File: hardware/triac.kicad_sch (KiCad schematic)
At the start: 23 parts, among them Q2 BTA16-600B, Q3 BC848, U4 TL082

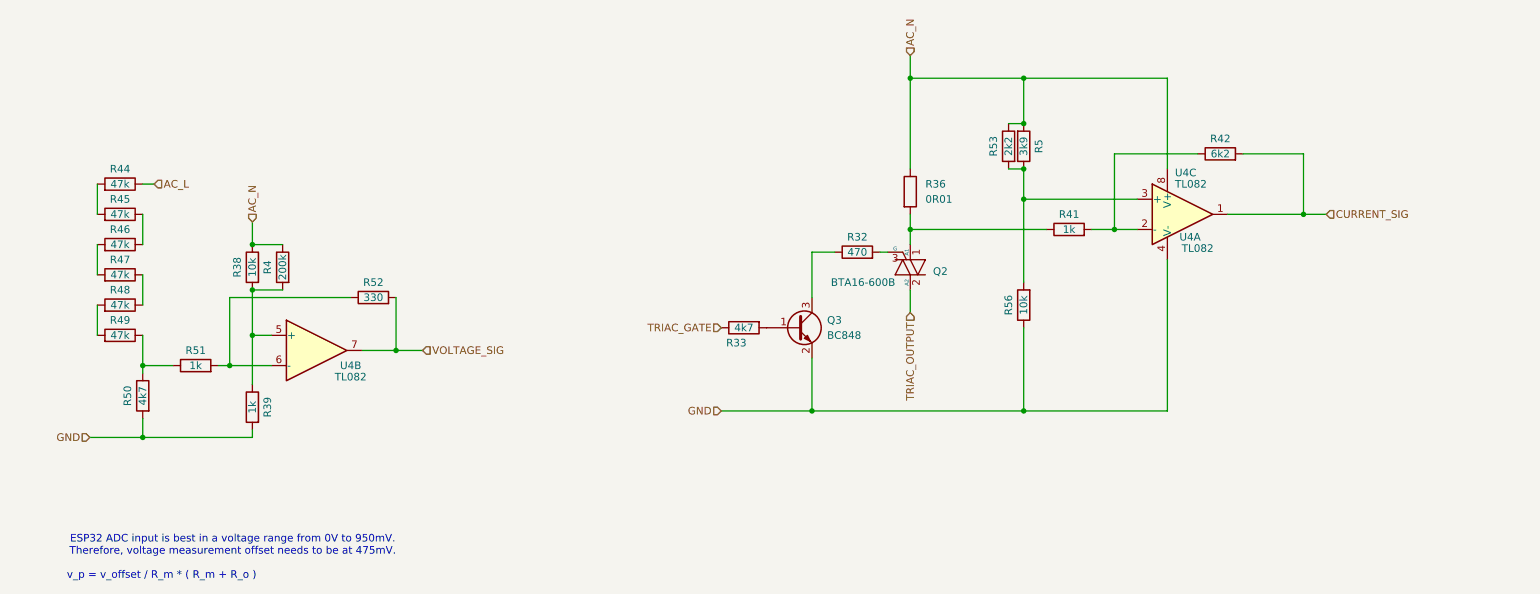
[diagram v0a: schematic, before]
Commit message: bugfix: triac output needs to confront L potential
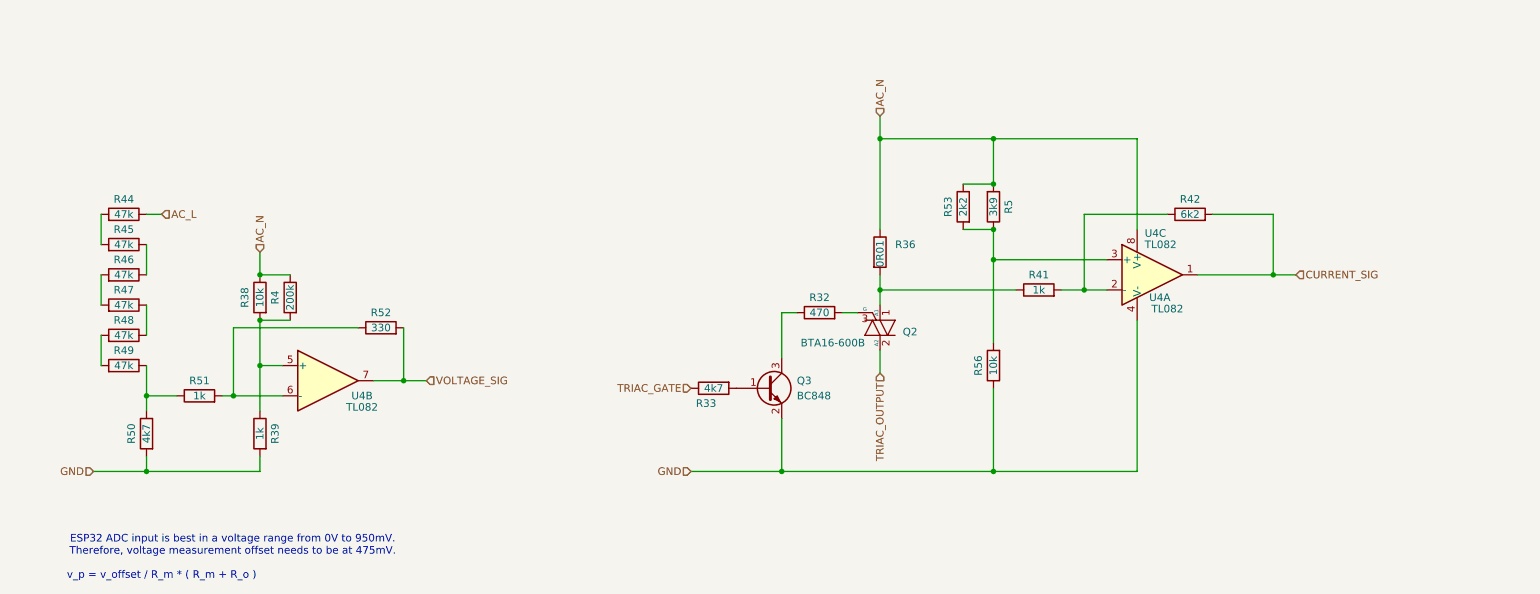
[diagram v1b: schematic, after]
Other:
- moved on the sheet: Q2, Q3, R32, R33, R36, R38, R39, R4, R41, R42, R44, R45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

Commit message: added some datasheets
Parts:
- removed R44, R45, R46, R47, R48, R49: 47k, Resistor_SMD:R_0603_1608Metric, symbol Device:R
- added R6: 270k, Resistor_SMD:R_MELF_MMB-0207, symbol Device:R
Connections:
- net AC_L: now also R6.1
- net at R50.1, R51.1: now also R6.2
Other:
- moved on the sheet: R36

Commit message: some more rules and routings
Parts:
- removed Q3: BC848, Package_TO_SOT_SMD:SOT-23, symbol Transistor_BJT:BC848
- removed R33: 4k7, Resistor_SMD:R_0603_1608Metric, symbol Device:R
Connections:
- net TRIAC_GATE: now also R32.1
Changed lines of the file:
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@@
-	)
-	(junction
-		(at 142.24 127)
-		(diameter 0)
-		(color 0 0 0 0)
 	)
 	(junction
@@
 	(wire
 		(pts
-			(xy 127 127) (xy 142.24 127)
+			(xy 140.97 127) (xy 177.8 127)
 		)
 		(stroke
@@
 	(wire
 		(pts
-			(xy 142.24 118.11) (xy 142.24 127)
-		)
-		(stroke
-			(width 0)
-			(type default)
-		)
-	)
-	(wire
-		(pts
 			(xy 158.75 71.12) (xy 177.8 71.12)
 		)
@@
 	(wire
 		(pts
-			(xy 142.24 127) (xy 177.8 127)
-		)
-		(stroke
-			(width 0)
-			(type default)
-		)
-	)
-	(wire
-		(pts
 			(xy 158.75 71.12) (xy 158.75 80.01)
 		)
@@
 		(pts
 			(xy 35.56 114.3) (xy 35.56 116.84)
-		)
-		(stroke
-			(width 0)
-			(type default)
-		)
-	)
-	(wire
-		(pts
-			(xy 142.24 100.33) (xy 142.24 107.95)
 		)
 		(stroke
@@
 	(hierarchical_label "GND"
 		(shape input)
-		(at 127 127 180)
+		(at 140.97 127 180)
 		(fields_autoplaced yes)
 		(effects
@@
 	(hierarchical_label "TRIAC_GATE"
 		(shape input)
-		(at 127 113.03 180)
+		(at 142.24 100.33 180)
 		(fields_autoplaced yes)
 		(effects
@@
 	)
 	(symbol
-		(lib_id "Transistor_BJT:BC848")
-		(at 139.7 113.03 0)
-		(unit 1)
-		(exclude_from_sim no)
-		(in_bom yes)
-		(on_board yes)
-		(dnp no)
-		(fields_autoplaced yes)
-		(property "Reference" "Q3"
-			(at 144.78 111.7599 0)
-			(effects
-				(font
-					(size 1.27 1.27)
-				)
-				(justify left)
-			)
-		)
-		(property "Value" "BC848"
-			(at 144.78 114.2999 0)
-			(effects
-				(font
-					(size 1.27 1.27)
-				)
-				(justify left)
-			)
-		)
-		(property "Footprint" "Package_TO_SOT_SMD:SOT-23"
-			(at 144.78 114.935 0)
-			(effects
-				(font
-					(size 1.27 1.27)
-					(italic yes)
-				)
-				(justify left)
-				(hide yes)
-			)
-		)
-		(property "Datasheet" "http://www.infineon.com/dgdl/Infineon-BC847SERIES_BC848SERIES_BC849SERIES_BC850SERIES-DS-v01_01-en.pdf?fileId=db3a304314dca389011541d4630a1657"
-			(at 139.7 113.03 0)
-			(effects
-				(font
-					(size 1.27 1.27)
-				)
-				(justify left)
-				(hide yes)
-			)
-		)
-		(property "Description" ""
-			(at 139.7 113.03 0)
-			(effects
-				(font
-					(size 1.27 1.27)
-				)
-				(hide yes)
-			)
-		)
-		(pin "1"
-		)
-		(pin "2"
-		)
-		(pin "3"
-		)
-		(instances
-			(project "Steuerplatine"
-				(path "/ae153005-c1c4-4678-92de-98a47cf88e8d/3bec7522-070b-49c2-9368-07aeb74f76c4"
-					(reference "Q3")
-					(unit 1)
-				)
-			)
-		)
-	)
-	(symbol
 		(lib_id "Device:R")
 		(at 35.56 120.65 0)
@@
 					(unit 1)
 				)
-			)
-		)
-	)
-	(symbol
-		(lib_id "Device:R")
-		(at 130.81 113.03 90)
-		(mirror x)
-		(unit 1)
-		(exclude_from_sim no)
-		(in_bom yes)
-		(on_board yes)
-		(dnp no)
-		(property "Reference" "R33"
-			(at 129.54 115.57 90)
-			(effects
-				(font
-					(size 1.27 1.27)
-				)
-			)
-		)
-		(property "Value" "4k7"
-			(at 130.81 113.03 90)
-			(effects
-				(font
-					(size 1.27 1.27)
-				)
-			)
-		)
-		(property "Footprint" "Resistor_SMD:R_0603_1608Metric"
-			(at 130.81 111.252 90)
-			(effects
-				(font
-					(size 1.27 1.27)
-				)
-				(hide yes)
-			)
-		)
-		(property "Datasheet" "~"
-			(at 130.81 113.03 0)
-			(effects
-				(font
-					(size 1.27 1.27)
-				)
-				(hide yes)
-			)
-		)
-		(property "Description" ""
-			(at 130.81 113.03 0)
-			(effects
-				(font
-					(size 1.27 1.27)
-				)
-				(hide yes)
-			)
-		)
-		(pin "1"
-		)
-		(pin "2"
-		)
-		(instances
-			(project "Steuerplatine"
-				(path "/ae153005-c1c4-4678-92de-98a47cf88e8d/3bec7522-070b-49c2-9368-07aeb74f76c4"
-					(reference "R33")
-					(unit 1)
-				)

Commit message: added gnd layer
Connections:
- net AC_N: no longer U4.8 (V+)
- new net +3V3: U4.8 (V+)
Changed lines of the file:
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@@
 	(paper "A4")
 	(junction
-		(at 177.8 71.12)
-		(diameter 0)
-		(color 0 0 0 0)
-	)
-	(junction
 		(at 54.61 101.6)
 		(diameter 0)
@@
 		(pts
 			(xy 35.56 124.46) (xy 35.56 127)
-		)
-		(stroke
-			(width 0)
-			(type default)
-		)
-	)
-	(wire
-		(pts
-			(xy 177.8 71.12) (xy 201.93 71.12)
 		)
 		(stroke
@@
 		)
 	)
+	(hierarchical_label "+3V3"
+		(shape input)
+		(at 201.93 71.12 90)
+		(fields_autoplaced yes)
+		(effects
+			(font
+				(size 1.27 1.27)
+			)
+			(justify left)
+		)
+	)

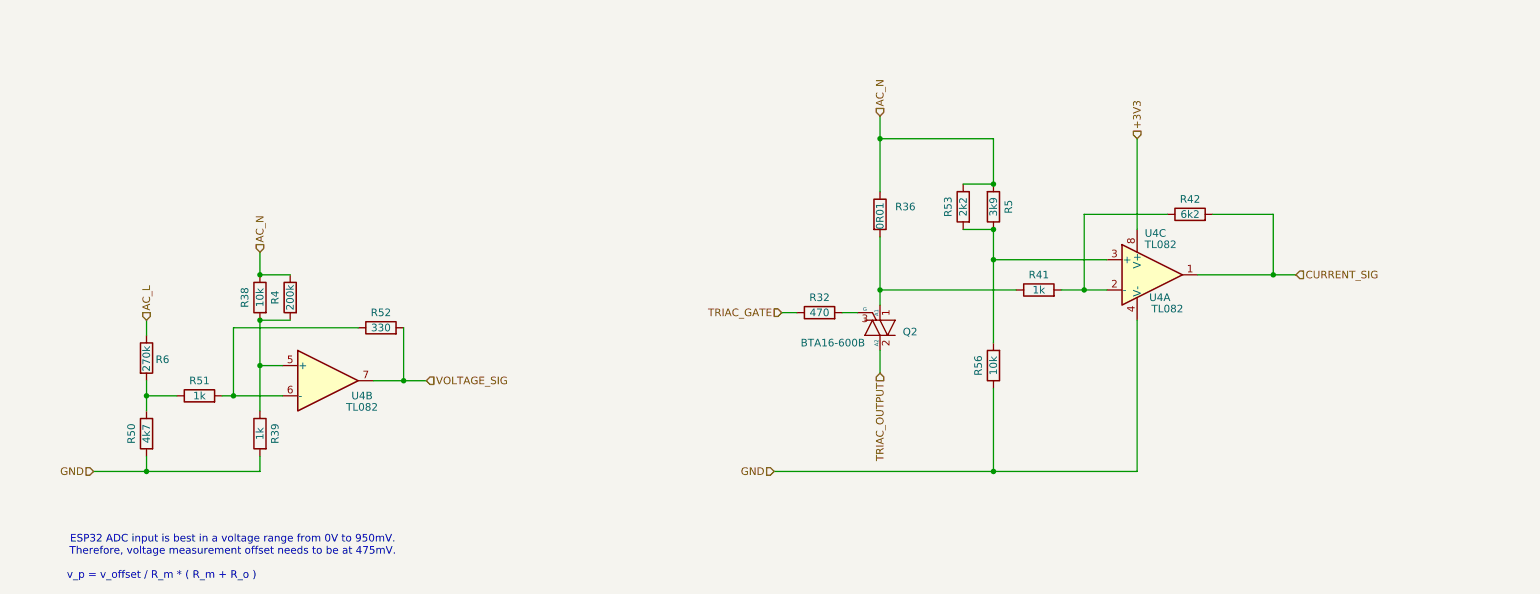
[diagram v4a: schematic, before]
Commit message: added testpoints. adjusted opamps for correct measurement. replaced hard resistors with potentiometer trimmers if necessary
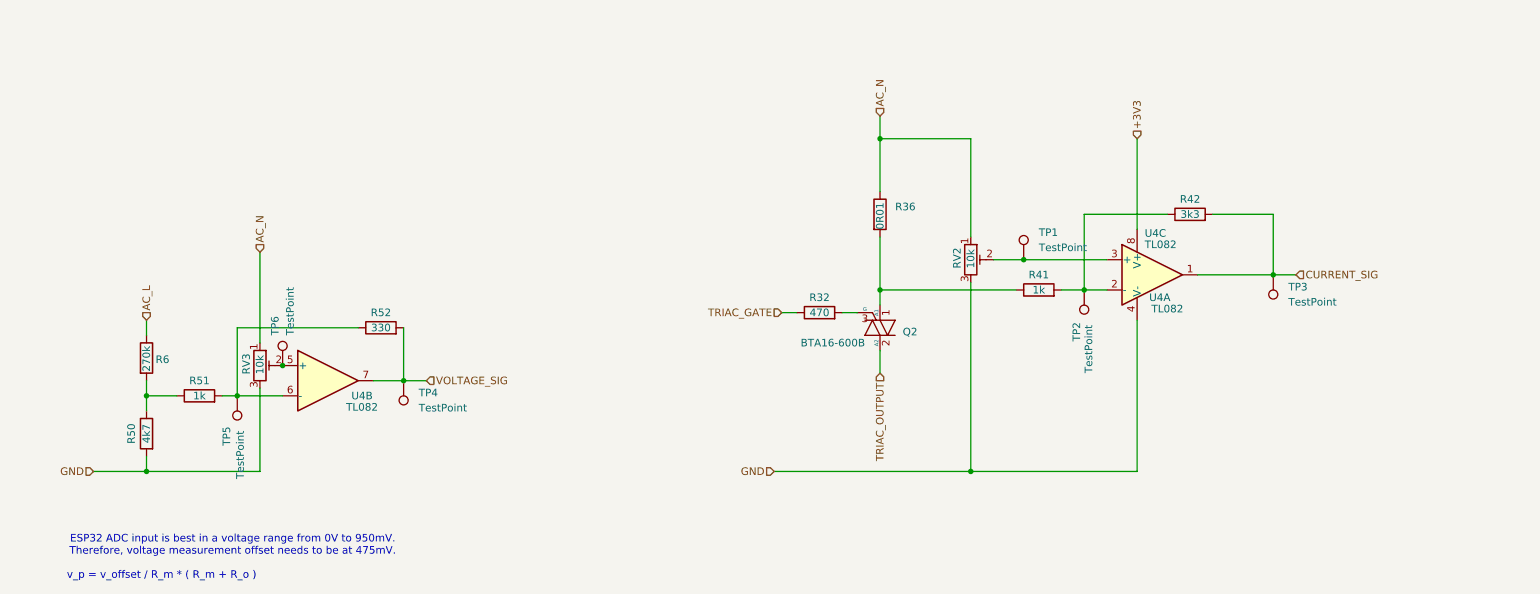
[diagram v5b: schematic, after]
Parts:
- removed R38, R56: 10k, Resistor_SMD:R_0603_1608Metric, symbol Device:R
- removed R39: 1k, Resistor_SMD:R_0603_1608Metric, symbol Device:R
- removed R4: 200k, Resistor_SMD:R_0603_1608Metric, symbol Device:R
- removed R5: 3k9, Resistor_SMD:R_0603_1608Metric, symbol Device:R
- removed R53: 2k2, Resistor_SMD:R_0603_1608Metric, symbol Device:R
- added RV2, RV3: 10k, Potentiometer_THT:Potentiometer_Bourns_3299W_Vertical, symbol Device:R_Potentiometer_Trim
- added TP1, TP2, TP3, TP4, TP5, TP6: TestPoint, TestPoint:TestPoint_Pad_D1.0mm, symbol Connector:TestPoint
- R42: value 6k2 -> 3k3
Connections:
- net AC_N: now also RV2.1, RV3.1
- net CURRENT_SIG: now also TP3.1
- net GND: now also RV2.3, RV3.3
- net VOLTAGE_SIG: now also TP4.1
- net at R51.2, R52.1, U4.6 (-): now also TP5.1
- net at U4.5 (+): now also RV3.2, TP6.1
- net at U4.3 (+): now also RV2.2, TP1.1
- net at R41.2, R42.1, U4.2 (-): now also TP2.1

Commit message: changed opamp for a rail-to-rail device. bugfix: got the right package for phoenix mstba outlets. beauty: rearranged some test points for better visibility. bugfix: added bypass diodes to analog output to protect adc on chip
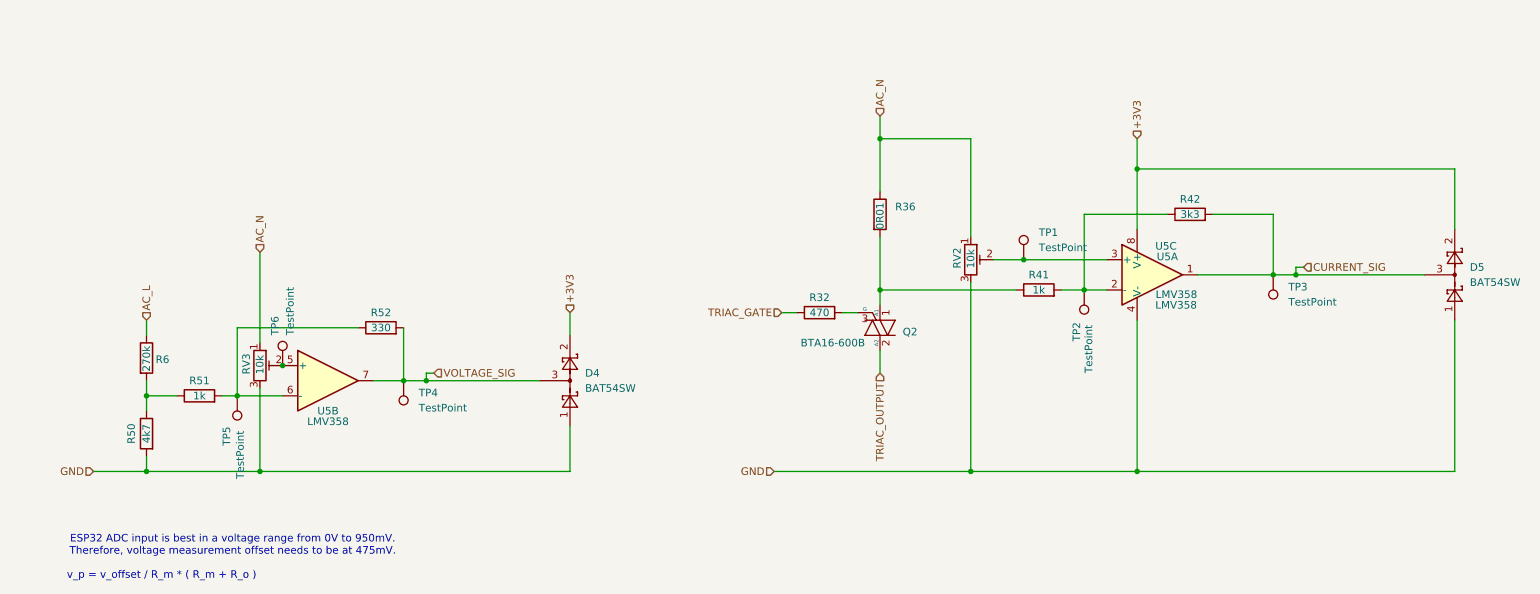
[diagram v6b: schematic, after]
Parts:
- removed U4: TL082, Package_SO:SO-8_5.3x6.2mm_P1.27mm, symbol Amplifier_Operational:TL082
- added D4, D5: BAT54SW, Package_TO_SOT_SMD:SOT-23, symbol Diode:BAT54SW
- added U5: LMV358, Package_SO:SOIC-8_3.9x4.9mm_P1.27mm, symbol Amplifier_Operational:LMV358
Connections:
- net +3V3: now also D4.2, D5.2, U5.8 (V+)
- net CURRENT_SIG: now also D5.3, U5.1
- net GND: now also D4.1, D5.1, U5.4 (V-)
- net VOLTAGE_SIG: now also D4.3, U5.7
- net at R51.2, R52.1, TP5.1: now also U5.6 (-)
- net at RV2.2, TP1.1: now also U5.3 (+)
- net at R41.2, R42.1, TP2.1: now also U5.2 (-)
- net at RV3.2, TP6.1: now also U5.5 (+)
